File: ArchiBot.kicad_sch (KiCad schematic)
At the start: 124 parts, among them J1 Power, J10 Header 3P 2.54mm, J11 Header 3P 2.54mm, J12 Header 3P 2.54mm, J13 Header 3P 2.54mm, J14 Header 3P 2.54mm, J15 Bornera 2P 5mm_1, J16 Bornera 2P 5mm_1, J17 Bornera 2P 5mm_1, J18 Bornera 2P 5mm_1, J19 Header 3P 2.54mm, J2 Digital/PWM, J20 Header 3P 2.54mm, J21 Header 3P 2.54mm, J22 Header 3P 2.54mm, J23 Header 3P 2.54mm, J24 V+EXT, J25 Header 3P 2.54mm, J26 Laser, J27 BATin, J28 M1, J29 M2, J3 Analog, J30 M3, J31 M4, J32 LASER, J33 POWER_JMP, J34 ADCs, J35 Bluetooth, J36 JMP18, J37 JMP03, J38 JMP04, J39 JMP05, J4 Digital/PWM, J40 JMP11, J41 GP03, J42 GP04, J43 GP04, J44 GP04, J45 GP04, J46 GP04, J47 GP04, J48 GP04, J49 GP04, J5 Header 3P 2.54mm, J50 GP04, J6 Header 3P 2.54mm, J7 Header 3P 2.54mm, J8 Header 3P 2.54mm, J9 Header 3P 2.54mm, Q1 SMMBT3904LT1G, Q2 MMBT3904, U1 ShieldArchi, U10 TPS563252DRLR, U2 SN74HC595NSR, U3 L293DD, U4 1117-5.0, U5 L293DD, U6 L293DD, U7 L293DD, U8 74HC595, U9 RESET

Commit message: Reorganizo esquematico
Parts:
- removed ADC1: Header 4P 2.54mm, Header 4P 2.54mm, symbol ArchiBot-altium-import:root_0_mirrored_Header 4P 2.54mm
- removed BLUETOOTH1: HEADER_6_VIAS, HEADER_6_VIAS, symbol ArchiBot-altium-import:root_0_HEADER_6_VIAS
- removed C1, C6: 100uF/25V, PNSC-FK-V-D8_V, symbol ArchiBot-altium-import:root_0_CAP-P-2
- removed C10, C3, C8: 0.1uF/16V 0603, FP-CC0603-DA-MFG, symbol ArchiBot-altium-import:root_0_11868f565c42a9108669ba33697ecf6
- removed C2, C7: 100uF/10V, FP-SC-MFG, symbol ArchiBot-altium-import:root_0_a00bbbee19879c290e62620ae7e47b1
- removed C4: 1nF, FP-C2012-125-0_2-IPC_B, symbol ArchiBot-altium-import:root_0_b4654b650e69147ec39a6b967a45e02
- removed C5, C9: 47uF/35V, FP-FPD-MFG, symbol ArchiBot-altium-import:root_0_cf48714ba7e38822c1575c7ec0b6d1f
- removed J10, J11, J12, J13, J14, J19, J20, J21, J22, J23, J5, J6, J7, J8, J9: Header 3P 2.54mm, Header 3P 2.54mm, symbol ArchiBot-altium-import:root_0_mirrored_Header 3P 2.54mm
- removed J15, J16, J17, J18: Bornera 2P 5mm_1, PHOE-1729128-2_V, symbol ArchiBot-altium-import:root_0_mirrored_Bornera 2P 5mm_1
- removed J24: V+EXT, PHOE-1729128-2_V, symbol ArchiBot-altium-import:root_0_mirrored_Bornera 2P 5mm
- removed J25: Header 3P 2.54mm, Header 3P 2.54mm, symbol ArchiBot-altium-import:root_1_Header 3P 2.54mm
- removed J26: Laser, SAMTEC-HTSW-102-07-X-S, symbol ArchiBot-altium-import:root_0_Header 2P 2.54mm
- removed Led1: ~, WL-SMCW_1206_150120xx75000, symbol ArchiBot-altium-import:root_3_LED_Red_2A-1K
- removed Q1: SMMBT3904LT1G, ONSC-SOT-23-3-318-08_V - duplicate, symbol ArchiBot-altium-import:root_0_CMP-1048-00625-1
- removed R1, R10: 10K, FP-MCU0805-IPC_C, symbol ArchiBot-altium-import:root_3_1029c3af85768c4190bb7ad29bc67b5
- removed R11: 220R, FP-CRCW0603-e3-IPC_A, symbol ArchiBot-altium-import:root_1_CMP-2000-03062-2
- removed R12: 1k, FP-CRCW0603-e3-MFG, symbol ArchiBot-altium-import:root_0_1029c3af85768c4190bb7ad29bc67b5
- removed R2, R3, R4, R5, R6, R7, R8, R9: 10K, FP-MCU0805-IPC_C, symbol ArchiBot-altium-import:root_2_1029c3af85768c4190bb7ad29bc67b5
- removed RUN1: RUN, SWITCH PTS645, symbol ArchiBot-altium-import:root_0_SWITCH_1
- removed U1: ShieldArchi, ShieldArchi, symbol ArchiBot-altium-import:root_0_ShieldArchi
- removed U2: SN74HC595NSR, NS0016A_L, symbol ArchiBot-altium-import:root_0_CMP-0780-00160-3
- removed U3, U5: L293DD, STM-SOIC-20_M, symbol ArchiBot-altium-import:root_0_CMP-1771-00003-1
- removed U4: 1117-5.0, SOT-223, symbol ArchiBot-altium-import:root_0_1117-5.0
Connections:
- net GP02 is gone; now on net DIR_LATCH: J4.8 (Pin_8)
- net GP06 is gone; now on net DIR_CLK: J4.4 (Pin_4)
- net GP07 is gone; now on net DIR_SER: J4.3 (Pin_3)
- net GP08 is gone; now on net RX: J35.5 (Pin_5), J4.2 (Pin_2)
- net GP09 is gone; now on net TX: J35.4 (Pin_4), J4.1 (Pin_1)
- net GP12 renamed LASER
- no-connect marks 13 -> 6
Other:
- moved on the sheet: C13, C14, C15, C16, C17, C18, C19, C20, C21, C22, C23, C24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

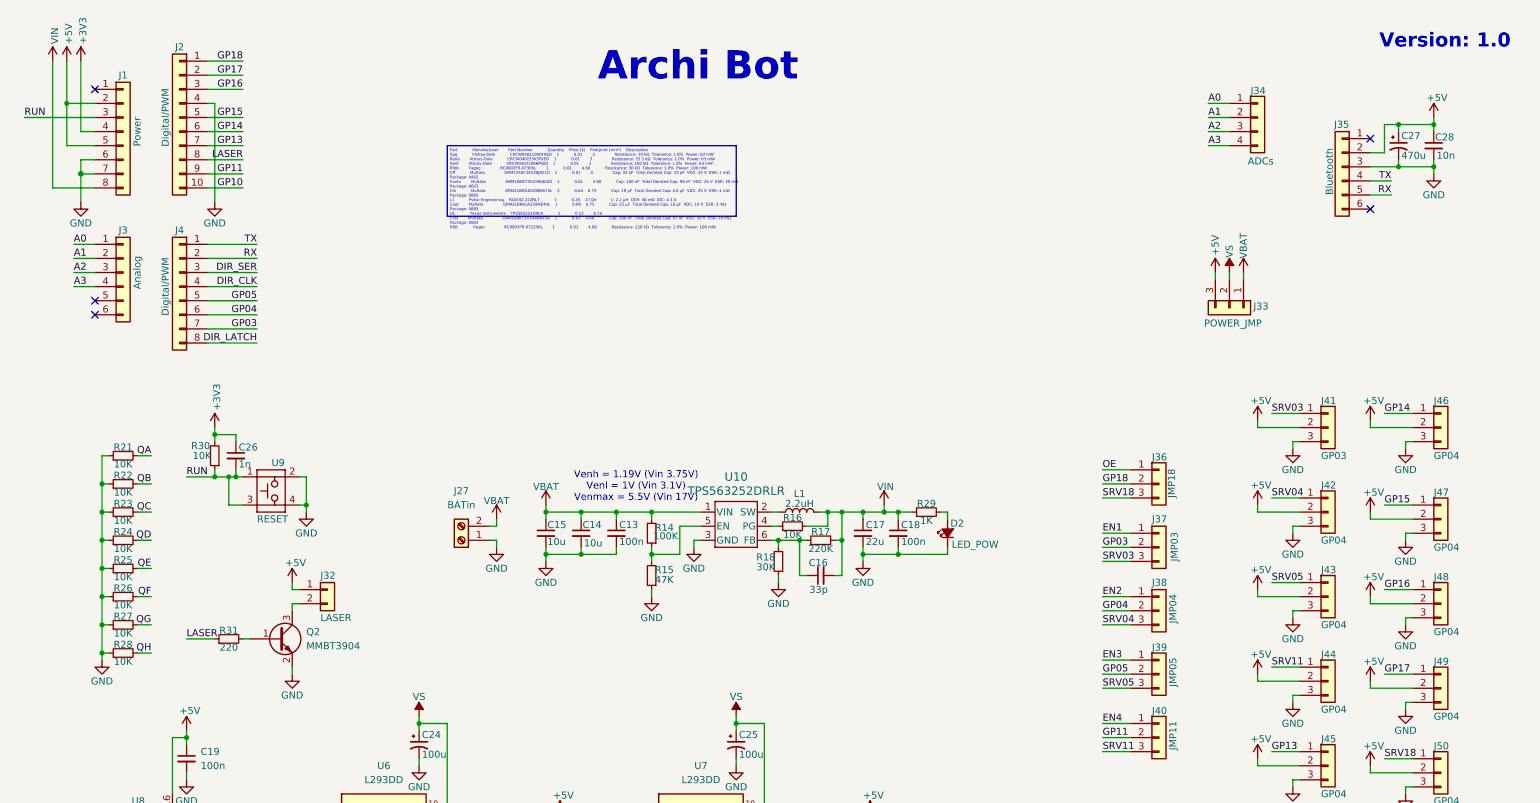
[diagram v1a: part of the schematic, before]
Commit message: Finalizo asignacion de footprints
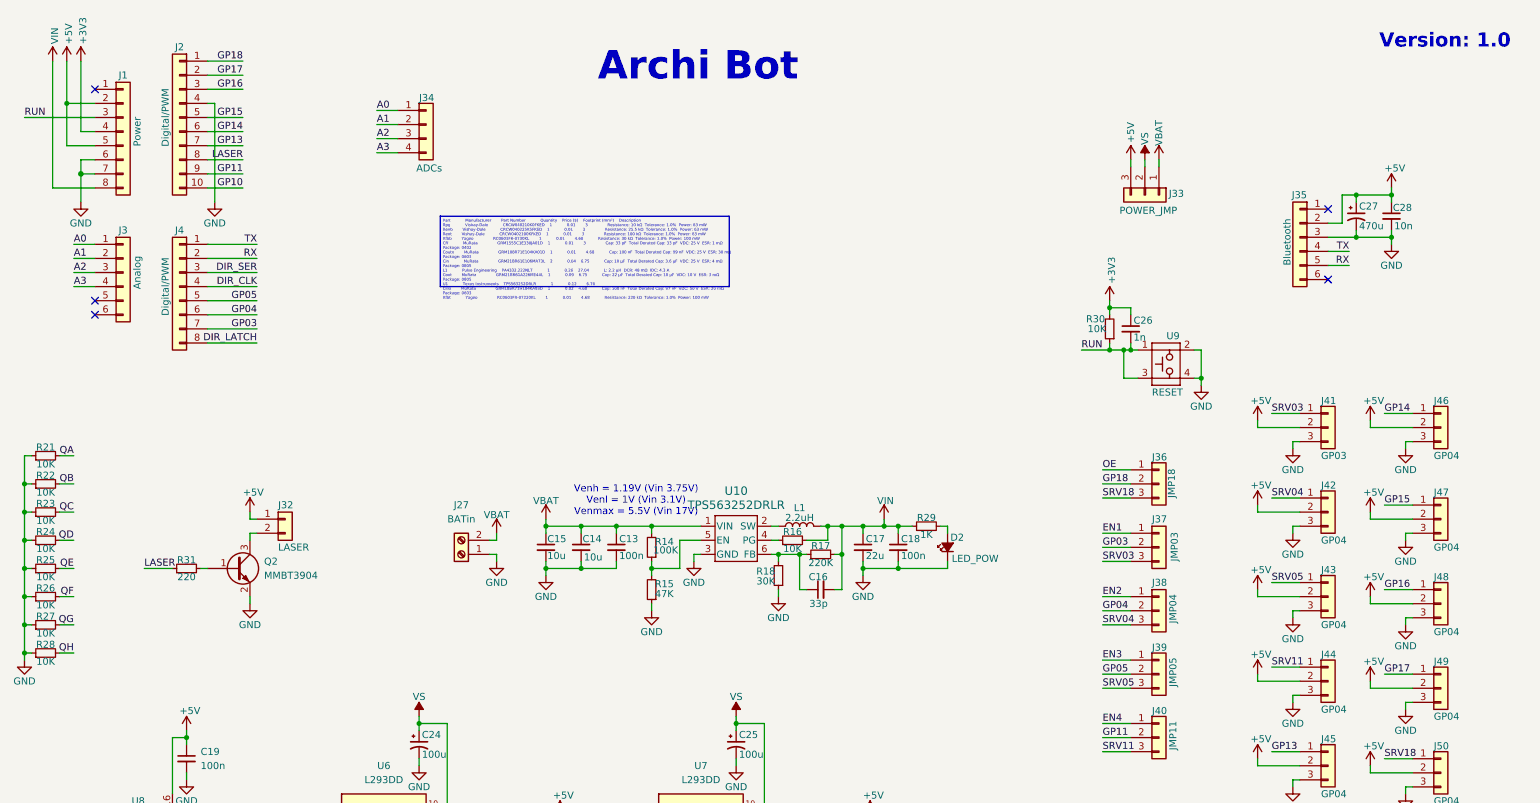
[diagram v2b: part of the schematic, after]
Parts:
- C13, C16, C18, C19, C21, C23, C26, C28: footprint (none) -> Capacitor_SMD:C_0603_1608Metric_Pad1.08x0.95mm_HandSolder
- C14, C15, C17: footprint (none) -> Capacitor_SMD:C_0805_2012Metric_Pad1.18x1.45mm_HandSolder
- C20, C22, C24, C25, C27: footprint (none) -> Newsanlib:CAP_EEEFK1E101XP
- D2: footprint (none) -> LED_SMD:LED_0603_1608Metric_Pad1.05x0.95mm_HandSolder
- R14, R15, R16, R17, R18, R19, R20, R21, R22, R23, R24, R25, R26, R27, R28, R29, R30, R31: footprint (none) -> Resistor_SMD:R_0603_1608Metric_Pad0.98x0.95mm_HandSolder
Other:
- moved on the sheet: C13, C14, C15, C16, C17, C18, C26, C27, C28, D2, J27, J32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

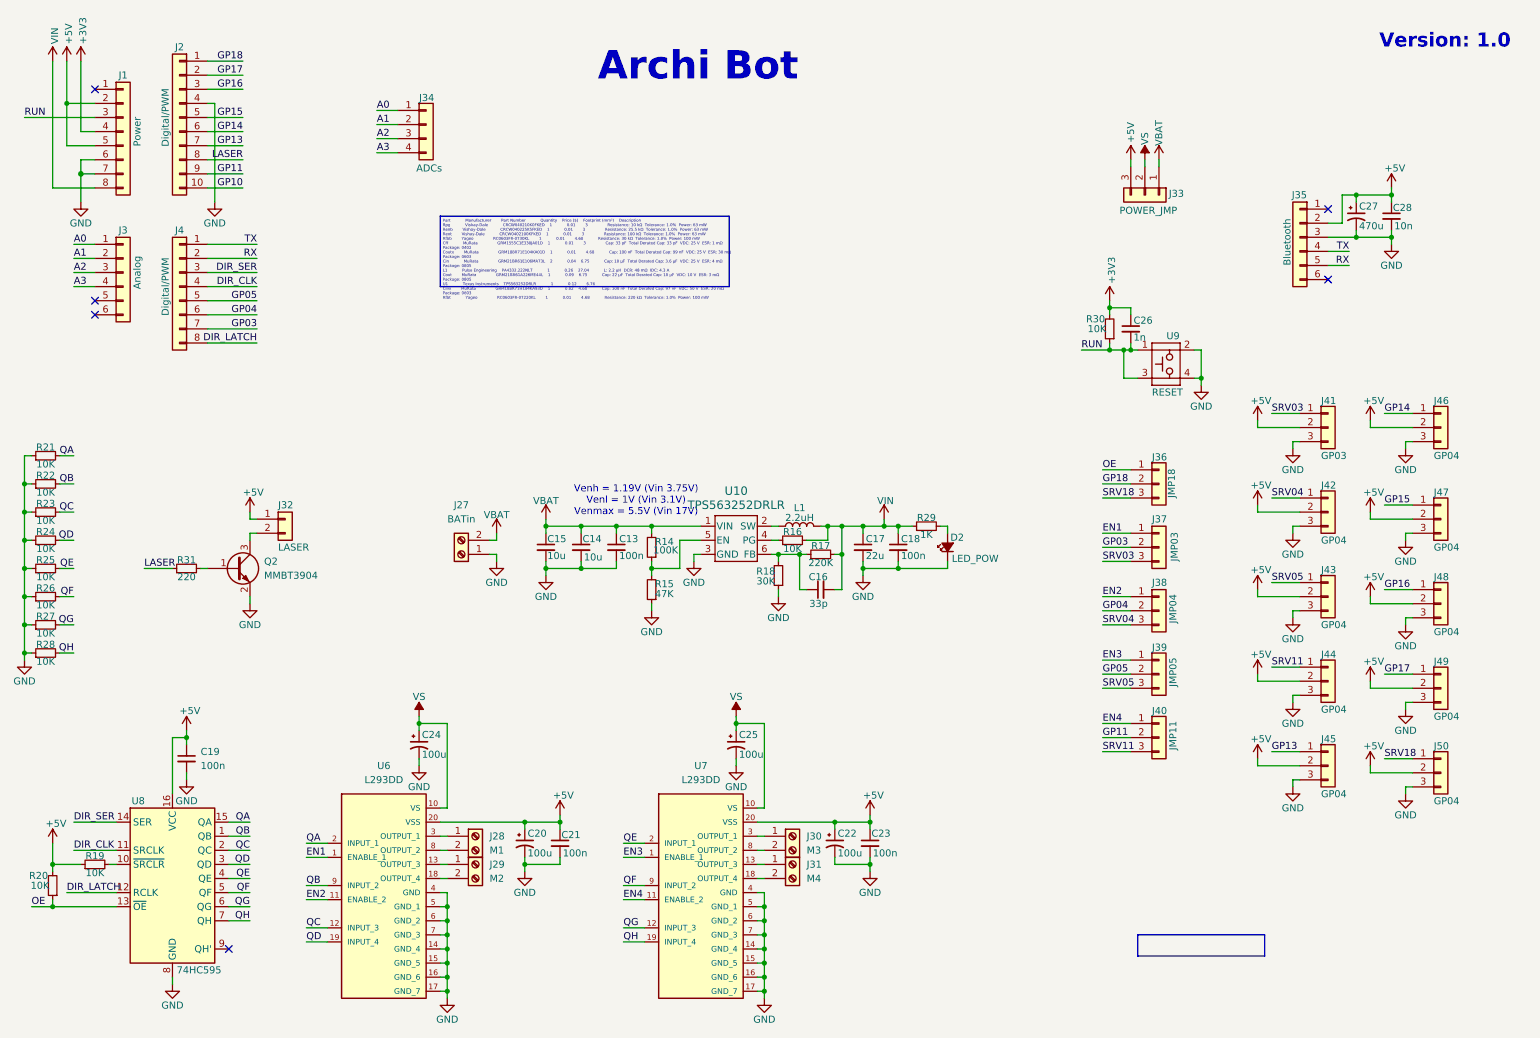
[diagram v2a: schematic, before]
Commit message: Separo el proyecto en hojas jerarquicas
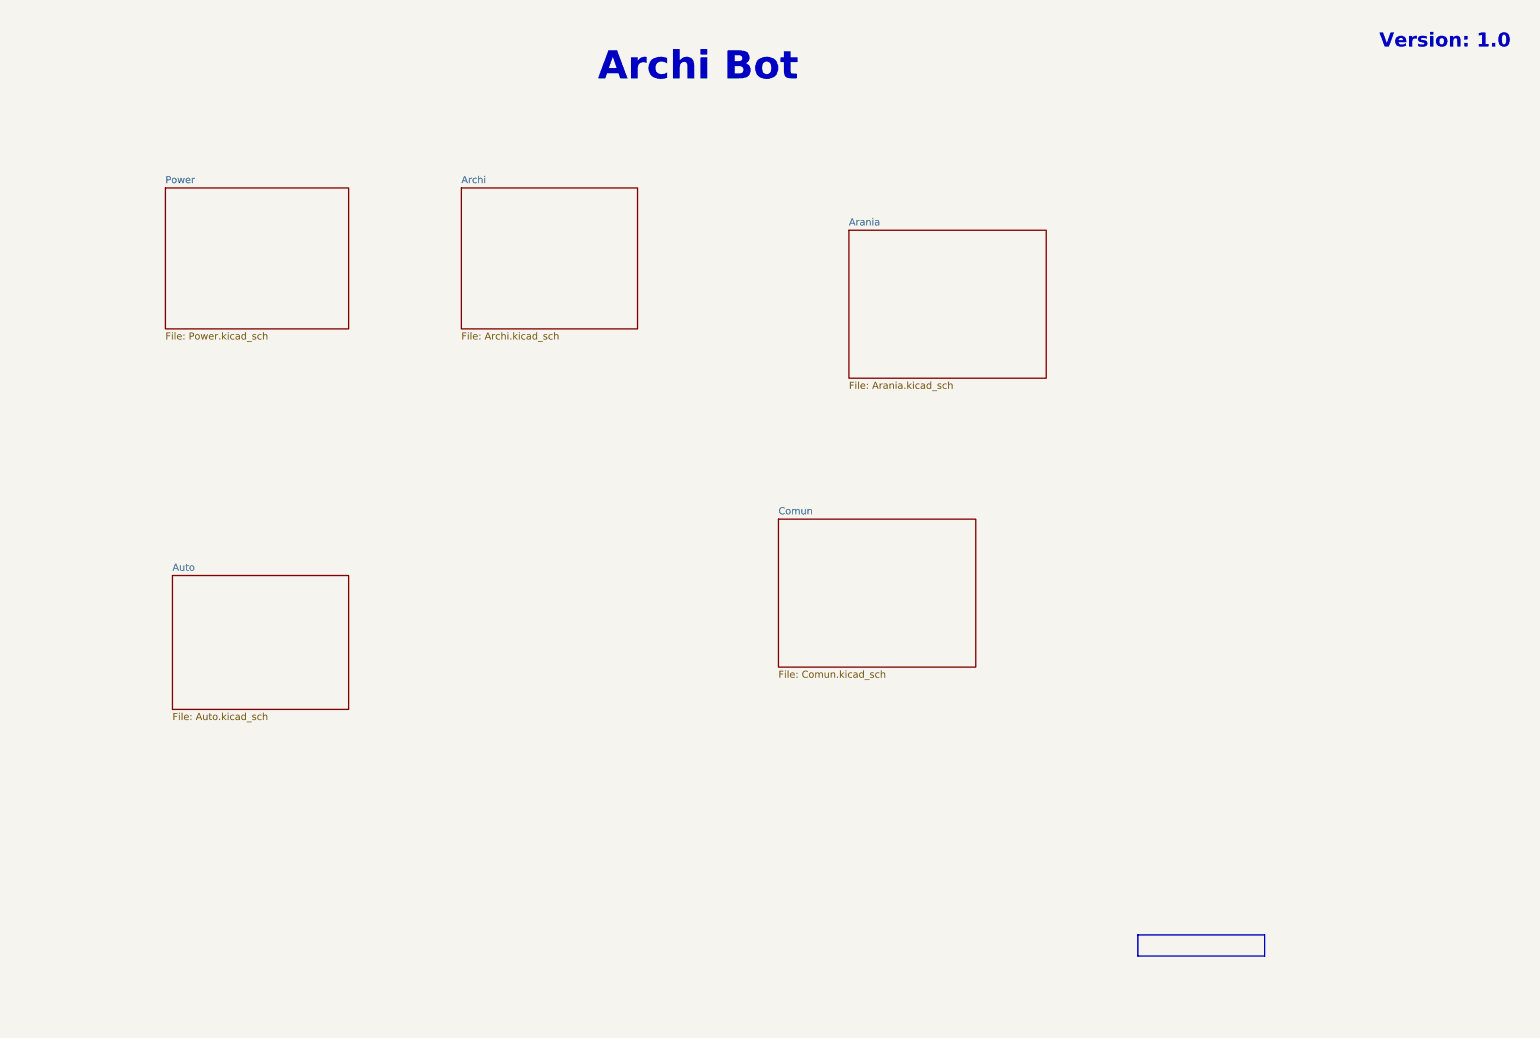
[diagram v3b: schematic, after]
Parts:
- removed C13, C18, C19, C21, C23: 100n, Capacitor_SMD:C_0603_1608Metric_Pad1.08x0.95mm_HandSolder, symbol Device:C_Small
- removed C14, C15: 10u, Capacitor_SMD:C_0805_2012Metric_Pad1.18x1.45mm_HandSolder, symbol Device:C_Small
- removed C16: 33p, Capacitor_SMD:C_0603_1608Metric_Pad1.08x0.95mm_HandSolder, symbol Device:C_Small
- removed C17: 22u, Capacitor_SMD:C_0805_2012Metric_Pad1.18x1.45mm_HandSolder, symbol Device:C_Small
- removed C20, C22, C24, C25: 100u, Newsanlib:CAP_EEEFK1E101XP, symbol Device:C_Polarized_Small_US
- removed C26: 1n, Capacitor_SMD:C_0603_1608Metric_Pad1.08x0.95mm_HandSolder, symbol Device:C_Small
- removed C27: 470u, Newsanlib:CAP_EEEFK1E101XP, symbol Device:C_Polarized_Small_US
- removed C28: 10n, Capacitor_SMD:C_0603_1608Metric_Pad1.08x0.95mm_HandSolder, symbol Device:C_Small
- removed D2: LED_POW, LED_SMD:LED_0603_1608Metric_Pad1.05x0.95mm_HandSolder, symbol Device:LED_Small_Filled
- removed J1: Power, Connector_PinHeader_2.54mm:PinHeader_1x08_P2.54mm_Vertical, symbol Connector_Generic:Conn_01x08
- removed J2: Digital/PWM, Connector_PinHeader_2.54mm:PinHeader_1x10_P2.54mm_Vertical, symbol Connector_Generic:Conn_01x10
- removed J27: BATin, TerminalBlock:TerminalBlock_bornier-2_P5.08mm, symbol Connector:Screw_Terminal_01x02
- removed J28: M1, TerminalBlock:TerminalBlock_bornier-2_P5.08mm, symbol Connector:Screw_Terminal_01x02
- removed J29: M2, TerminalBlock:TerminalBlock_bornier-2_P5.08mm, symbol Connector:Screw_Terminal_01x02
- removed J3: Analog, Connector_PinHeader_2.54mm:PinHeader_1x06_P2.54mm_Vertical, symbol Connector_Generic:Conn_01x06
- removed J30: M3, TerminalBlock:TerminalBlock_bornier-2_P5.08mm, symbol Connector:Screw_Terminal_01x02
- removed J31: M4, TerminalBlock:TerminalBlock_bornier-2_P5.08mm, symbol Connector:Screw_Terminal_01x02
- removed J32: LASER, Connector_PinHeader_1.27mm:PinHeader_1x02_P1.27mm_Vertical, symbol Connector_Generic:Conn_01x02
- removed J33: POWER_JMP, Connector_PinHeader_1.27mm:PinHeader_1x03_P1.27mm_Vertical, symbol Connector_Generic:Conn_01x03
- removed J34: ADCs, Connector_PinHeader_1.27mm:PinHeader_1x04_P1.27mm_Vertical, symbol Connector_Generic:Conn_01x04
- removed J35: Bluetooth, Connector_PinHeader_1.27mm:PinHeader_1x06_P1.27mm_Vertical, symbol Connector_Generic:Conn_01x06
- removed J36: JMP18, Connector_PinHeader_1.27mm:PinHeader_1x03_P1.27mm_Vertical, symbol Connector_Generic:Conn_01x03
- removed J37: JMP03, Connector_PinHeader_1.27mm:PinHeader_1x03_P1.27mm_Vertical, symbol Connector_Generic:Conn_01x03
- removed J38: JMP04, Connector_PinHeader_1.27mm:PinHeader_1x03_P1.27mm_Vertical, symbol Connector_Generic:Conn_01x03
- removed J39: JMP05, Connector_PinHeader_1.27mm:PinHeader_1x03_P1.27mm_Vertical, symbol Connector_Generic:Conn_01x03
- removed J4: Digital/PWM, Connector_PinHeader_2.54mm:PinHeader_1x08_P2.54mm_Vertical, symbol Connector_Generic:Conn_01x08
- removed J40: JMP11, Connector_PinHeader_1.27mm:PinHeader_1x03_P1.27mm_Vertical, symbol Connector_Generic:Conn_01x03
- removed J41: GP03, Connector_PinHeader_1.27mm:PinHeader_1x03_P1.27mm_Vertical, symbol Connector_Generic:Conn_01x03
- removed J42, J43, J44, J45, J46, J47, J48, J49, J50: GP04, Connector_PinHeader_1.27mm:PinHeader_1x03_P1.27mm_Vertical, symbol Connector_Generic:Conn_01x03
- removed L1: 2.2uH, Newsanlib:IND_PA4332.222NLT_PUL, symbol Device:L
- removed Q2: MMBT3904, Package_TO_SOT_SMD:SOT-23-3, symbol Transistor_BJT:MMBT3904
- removed R14: 100K, Resistor_SMD:R_0603_1608Metric_Pad0.98x0.95mm_HandSolder, symbol Device:R_Small
- removed R15: 47K, Resistor_SMD:R_0603_1608Metric_Pad0.98x0.95mm_HandSolder, symbol Device:R_Small
- removed R16, R19, R20, R21, R22, R23, R24, R25, R26, R27, R28, R30: 10K, Resistor_SMD:R_0603_1608Metric_Pad0.98x0.95mm_HandSolder, symbol Device:R_Small
- removed R17: 220K, Resistor_SMD:R_0603_1608Metric_Pad0.98x0.95mm_HandSolder, symbol Device:R_Small
- removed R18: 30K, Resistor_SMD:R_0603_1608Metric_Pad0.98x0.95mm_HandSolder, symbol Device:R_Small
- removed R29: 1K, Resistor_SMD:R_0603_1608Metric_Pad0.98x0.95mm_HandSolder, symbol Device:R_Small
- removed R31: 220, Resistor_SMD:R_0603_1608Metric_Pad0.98x0.95mm_HandSolder, symbol Device:R_Small
- removed U10: TPS563252DRLR, Newsanlib:SOT6_DRL_TEX-L, symbol Newsanlib:TPS563252DRLR
- removed U6, U7: L293DD, Newsanlib:SOIC127P1032X265-20N, symbol Newsanlib:L293DD
- removed U8: 74HC595, Package_SO:SOIC-16W_5.3x10.2mm_P1.27mm, symbol 74xx:74HC595
- removed U9: RESET, Newsanlib:SWITCH_43SMTR92LFS, symbol Newsanlib:PTS645SM43SMTR92LFS
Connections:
- no-connect marks 6 -> 0
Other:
- added sheet Arania (Arania.kicad_sch)
- added sheet Archi (Archi.kicad_sch)
- added sheet Auto (Auto.kicad_sch)
- added sheet Comun (Comun.kicad_sch)
- added sheet Power (Power.kicad_sch)
- note removed: "Venh = 1.19V (Vin 3.75V) Venl = 1V (Vin 3.1V) Venmax = 5.5V (Vin 17V)"
